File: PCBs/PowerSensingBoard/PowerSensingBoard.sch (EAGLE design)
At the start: 12 parts

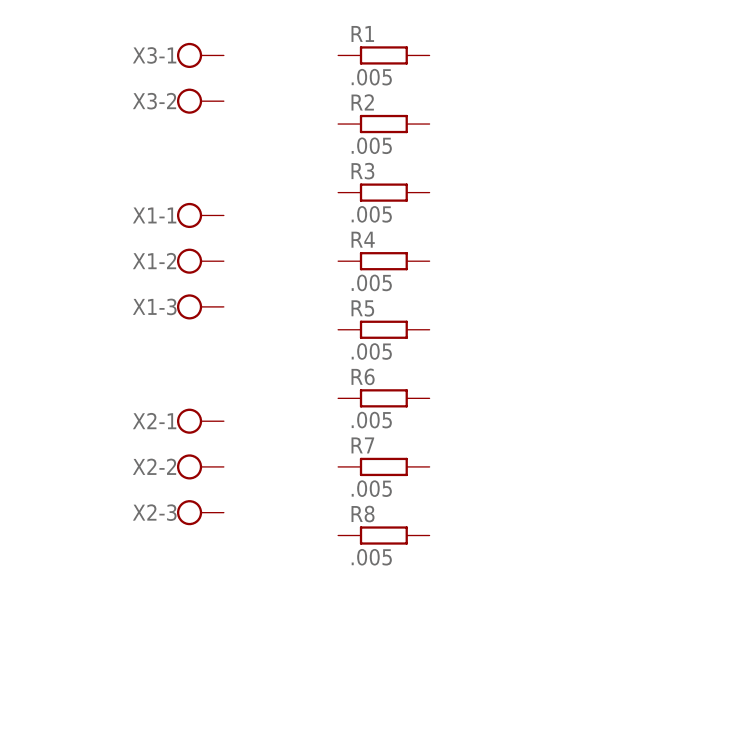
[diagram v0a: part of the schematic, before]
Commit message: Adding prelim sensing schematic
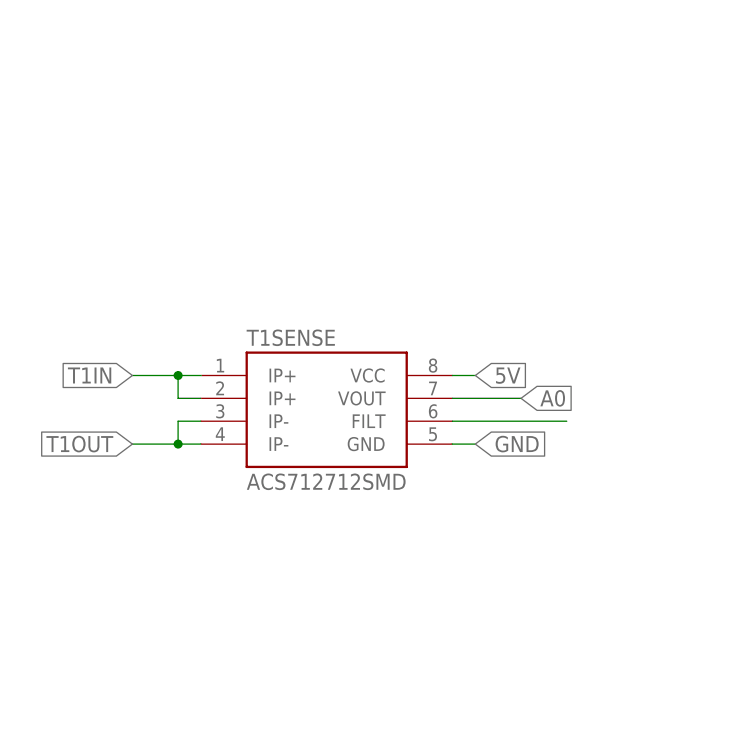
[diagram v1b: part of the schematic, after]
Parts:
- removed R1, R2, R3, R4, R5, R6, R7, R8: .005, resistor:R-EU_PRL1632
- removed X1, X2: (no value), con-wago-500:W237-103
- removed X3: (no value), con-wago-500:W237-102
- added T1SENSE: ACS712712SMD, SparkFun-AnalogIC:ACS712712SMD
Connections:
- new net 5V: T1SENSE.VCC
- new net A0: T1SENSE.VOUT
- new net FILT1: T1SENSE.FILT
- new net GND: T1SENSE.GND
- new net T1IN: T1SENSE.IP+@1, T1SENSE.IP+@2
- new net T1OUT: T1SENSE.IP-@3, T1SENSE.IP-@4

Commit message: Power Sensing board design
Power sensing rough draft of PCB almost done
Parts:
- removed T1SENSE: ACS712712SMD, SparkFun-AnalogIC:ACS712712SMD
- added C1, C2, C3, C4, C5, C6, C7, C8: 4.7uF, SparkFun-Capacitors:4.7UF-6.3V-10%(0603)0603
- added C10, C12, C14, C17: 10uF, SparkFun-Capacitors:4.7UF-6.3V-10%(0603)0603
- added C11, C13, C16, C9: .1uF, SparkFun-Capacitors:4.7UF-6.3V-10%(0603)0603
- added C15: 1uF, SparkFun-Capacitors:4.7UF-6.3V-10%(0603)0603
- added CSENSE0, CSENSE1, CSENSE2, CSENSE3, CSENSE4, CSENSE5, CSENSE6, CSENSE7: ACS712712SMD, SparkFun-AnalogIC:ACS712712SMD
- added IC1: 7805DT, adafruit:7805DT
- added R1: 1.5K, SparkFun-Resistors:1KOHM-1/10W-1%(0603)
- added R2: 1K, SparkFun-Resistors:1KOHM-1/10W-1%(0603)
- added U1: ATTINY84-20SSU, Atmel_By_element14_Batch_1-00:ATTINY84-20SSU
- added X1, X2, X3, X4, X5, X6, X7, X8: (no value), con-wago-500:W237-102
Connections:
- removed net T1IN: T1SENSE.IP+@1, T1SENSE.IP+@2
- removed net T1OUT: T1SENSE.IP-@3, T1SENSE.IP-@4
- new net A1: ADC1.CH1, CSENSE1.VOUT
- new net A2: ADC1.CH2, CSENSE2.VOUT
- new net A3: ADC1.CH3, CSENSE3.VOUT
- new net A4: ADC1.CH4, CSENSE4.VOUT
- new net A5: ADC1.CH5, CSENSE5.VOUT
- new net A6: ADC1.CH6, CSENSE6.VOUT
- new net A7: ADC1.CH7, CSENSE7.VOUT
- new net CLK: ADC1.SCK, U1.PA4
- new net CONVST: ADC1.CONVST
- new net FILT2: C2.1, CSENSE1.FILT
- new net FILT3: C3.1, CSENSE2.FILT
- new net FILT4: C4.1, CSENSE3.FILT
- new net FILT5: C5.1, CSENSE4.FILT
- new net FILT6: C6.1, CSENSE5.FILT
- new net FILT7: C7.1, CSENSE6.FILT
- new net FILT8: C8.1, CSENSE7.FILT
- new net INT1: CSENSE0.IP+@1, CSENSE0.IP+@2, X1-1.KL
- new net INT2: CSENSE1.IP+@1, CSENSE1.IP+@2, X2-1.KL
- new net INT3: CSENSE2.IP+@1, CSENSE2.IP+@2, X3-1.KL
- new net INT4: CSENSE3.IP+@1, CSENSE3.IP+@2, X4-1.KL
- new net INT5: CSENSE4.IP+@1, CSENSE4.IP+@2, X5-1.KL
- new net INT6: CSENSE5.IP+@1, CSENSE5.IP+@2, X6-1.KL
- new net INT7: CSENSE6.IP+@1, CSENSE6.IP+@2, X7-1.KL
- new net INT8: CSENSE7.IP+@1, CSENSE7.IP+@2, X8-1.KL
- new net MISO: ADC1.SDO, U1.PA5
- new net MOSI: ADC1.SDI, U1.PA6
- new net N$1: U1.PB2
- new net N$10: ADC1.DVDD, C11.1, C12.1
- new net N$11: ADC1.AVDO, C10.1, C9.1
- new net N$12: ADC1.VREF, C15.1
- new net N$13: ADC1.REFCOMP, C13.1, C14.1
- new net N$14: U1.PA7
- new net N$16: IC1.VI
- new net N$17: IC1.GND
- new net N$2: ADC1.MUXOUT+, R1.2
- new net N$3: ADC1.ADC+, R1.1, R2.2
- new net N$4: U1.GND
- new net N$5: ADC1.ADC-, ADC1.MUXOUT-
- new net N$6: U1.PA0
- new net N$7: U1.PA1
- new net N$8: U1.PA2
- new net OUTT1: CSENSE0.IP-@3, CSENSE0.IP-@4, X1-2.KL
- new net OUTT2: CSENSE1.IP-@3, CSENSE1.IP-@4, X2-2.KL
- new net OUTT3: CSENSE2.IP-@3, CSENSE2.IP-@4, X3-2.KL
- new net OUTT4: CSENSE3.IP-@3, CSENSE3.IP-@4, X4-2.KL
- new net OUTT5: CSENSE4.IP-@3, CSENSE4.IP-@4, X5-2.KL
- new net OUTT6: CSENSE5.IP-@3, CSENSE5.IP-@4, X6-2.KL
- new net OUTT7: CSENSE6.IP-@3, CSENSE6.IP-@4, X7-2.KL
- new net OUTT8: CSENSE7.IP-@3, CSENSE7.IP-@4, X8-2.KL
- new net RST: U1.PB3
- new net RX: U1.PB1
- new net TX: U1.PB0
- new net ~BUSY: ADC1.~BUSY, U1.PA3
- new net ~RD: ADC1.~RD
- net 5V: now also ADC1.OVDD, C16.1, C17.1, CSENSE0.VCC, CSENSE1.VCC, CSENSE2.VCC, CSENSE3.VCC, CSENSE4.VCC, CSENSE5.VCC, CSENSE6.VCC, CSENSE7.VCC, IC1.VO, U1.VCC; no longer T1SENSE.VCC
- net A0: now also ADC1.CH0, CSENSE0.VOUT; no longer T1SENSE.VOUT
- net FILT1: now also C1.1, CSENSE0.FILT; no longer T1SENSE.FILT
- net GND: now also ADC1.AGND1, ADC1.AGND2, ADC1.AGND3, ADC1.COM, ADC1.DGND, C1.2, C10.2, C11.2, C12.2, C13.2, C14.2, C15.2, C16.2, C17.2, C2.2, C3.2, C4.2, C5.2, C6.2, C7.2, C8.2, C9.2, CSENSE0.GND, CSENSE1.GND, CSENSE2.GND, CSENSE3.GND, CSENSE4.GND, CSENSE5.GND, CSENSE6.GND, CSENSE7.GND, R2.1; no longer T1SENSE.GND
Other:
- moved on the sheet: ADC1

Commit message: Current sensing progress
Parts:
- added J1: (no value), SparkFun-Connectors:PINHD-2X3
- added J2: (no value), SparkFun-Connectors:M02PTH
- added SV1: (no value), con-lstb:MA04-2
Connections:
- removed net N$1: U1.PB2
- removed net N$14: U1.PA7
- removed net N$16: IC1.VI
- removed net N$17: IC1.GND
- removed net N$6: U1.PA0
- removed net N$7: U1.PA1
- removed net N$8: U1.PA2
- new net 12V: IC1.VI, J2.1
- new net P0: SV1.2, U1.PA0
- new net P1: SV1.4, U1.PA1
- new net P2: SV1.6, U1.PA2
- net 5V: now also J1.2
- net CLK: now also J1.3
- net CONVST: now also SV1.5, U1.PB2
- net GND: now also IC1.GND, J1.6, J2.2
- net MISO: now also J1.1
- net MOSI: now also J1.4
- net RST: now also J1.5
- net RX: now also SV1.3
- net TX: now also SV1.1
- net ~BUSY: now also SV1.8
- net ~RD: now also SV1.7, U1.PA7
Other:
- moved on the sheet: ADC1, C10, C11, C12, C13, C14, C15, C16, C17, C9, IC1, R1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
